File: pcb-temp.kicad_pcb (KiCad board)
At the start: 2 copper layers, 15 parts, among them J1 Conn_01x04_Pin, J2 Conn_01x04_Pin, J3 Conn_01x06_Socket, J5 Conn_Coaxial_Small

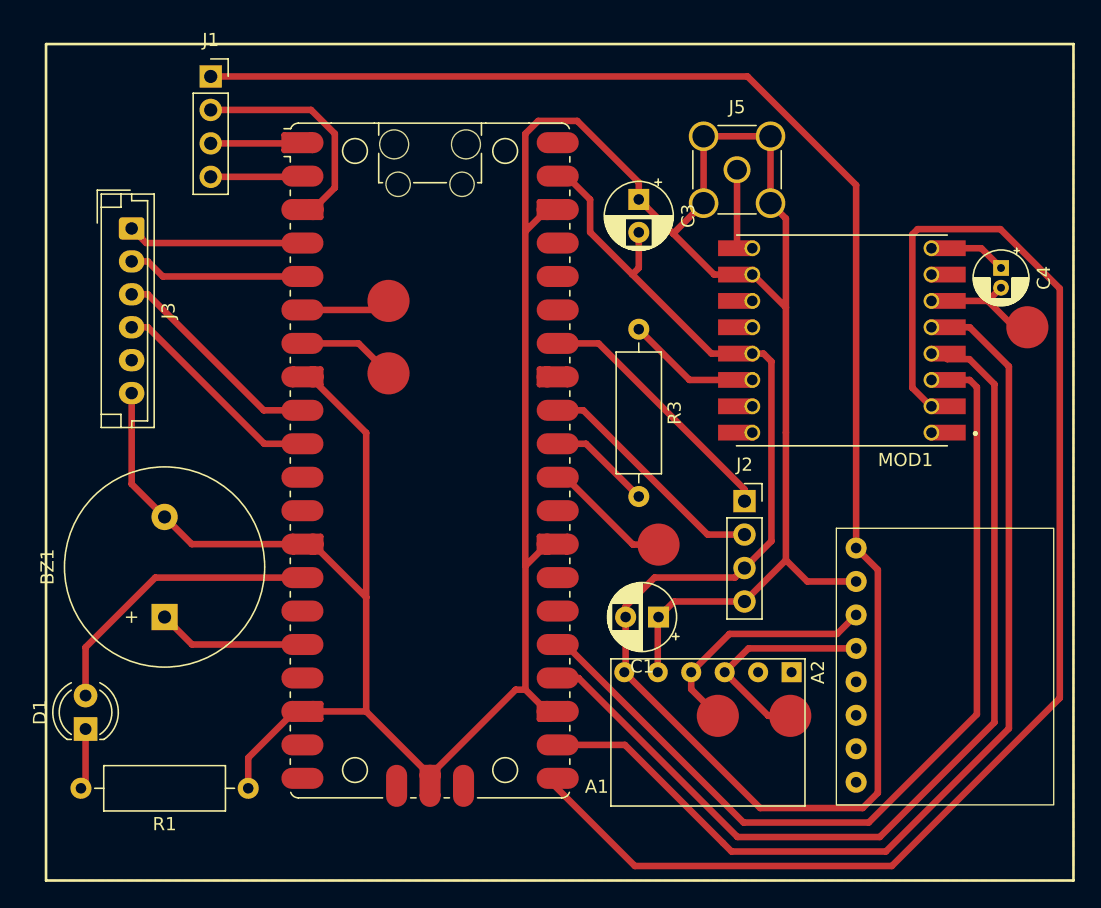
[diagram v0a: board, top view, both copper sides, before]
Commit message: thickened 3V3 path
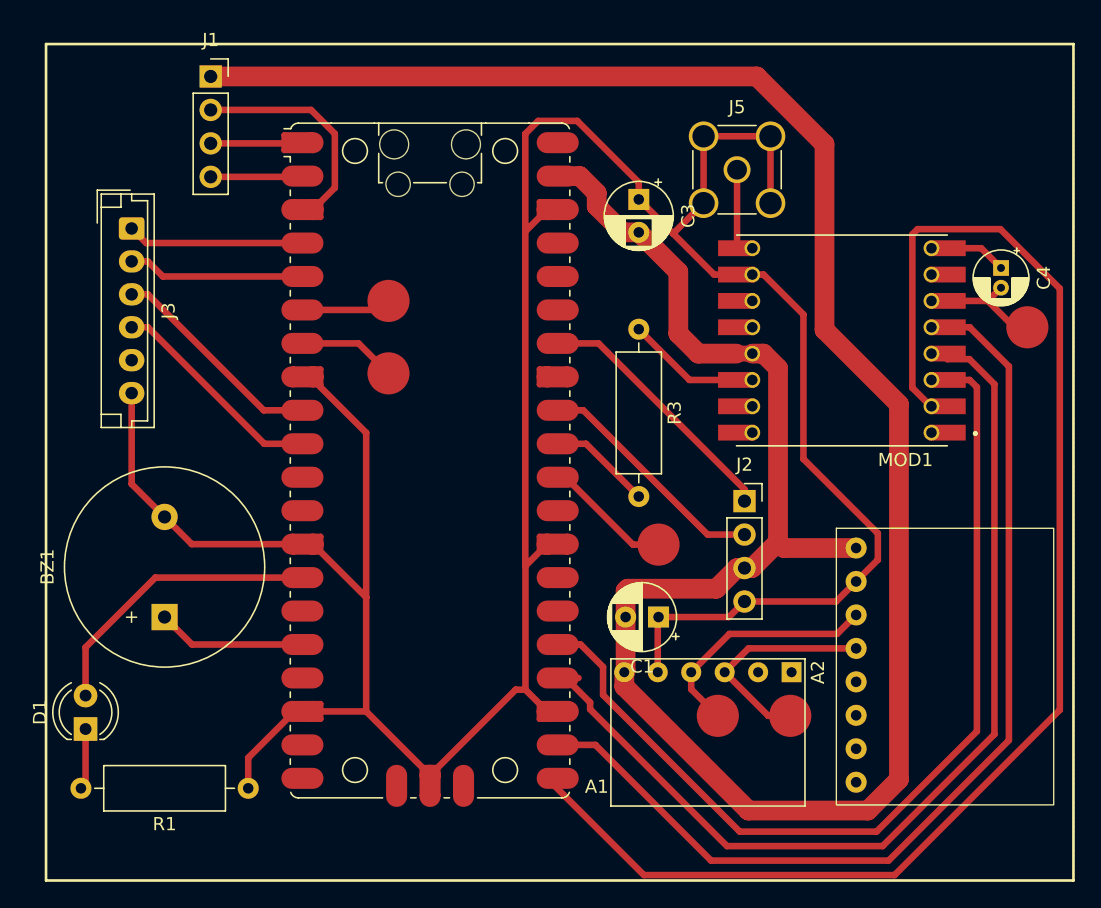
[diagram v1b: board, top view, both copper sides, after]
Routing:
- net +3V3: track 185.4 -> 195.8 mm
- net SPI SCK: track 73.2 -> 79.1 mm
- net GND: track 251.5 -> 247.4 mm
- net SPI MOSI: track 69.5 -> 72.1 mm
- net SPI MISO: track 104.9 -> 106.0 mm
- net SPI NSS: track 75.7 -> 76.8 mm
